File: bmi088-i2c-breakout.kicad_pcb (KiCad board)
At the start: 2 copper layers, 14.2 x 10.5 mm, 9 parts, among them J1 Conn_01x04_Socket, J2 Conn_01x04_Socket, U1 BMI088

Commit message: modified:   bmi088-i2c-breakout.kicad_pcb
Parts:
- moved JP2 2.15 mm to (150.4, 90.9)
- moved U1 0.25 mm to (152.1, 94.5)
- turned JP1 to 180 degrees
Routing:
- net /SCL: track 0.00 -> 15.6 mm, vias 0 -> 2
- net /3V3: track 0.00 -> 15.0 mm, vias 0 -> 2
- net Net-(JP1-B): track 0.00 -> 13.9 mm, vias 0 -> 2
- net /INT1: track 0.00 -> 11.5 mm, vias 0 -> 1
- net /SDA: track 0.00 -> 10.4 mm
- net /GND: track 0.00 -> 9.87 mm, vias 0 -> 2
- net /INT2: track 0.00 -> 9.02 mm, vias 0 -> 1
- net /INT4: track 0.00 -> 8.63 mm, vias 0 -> 1
- net /INT3: track 0.00 -> 8.31 mm, vias 0 -> 1
- net Net-(JP2-B): track 0.00 -> 6.58 mm
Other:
- board size 14.2 x 10.5 mm -> 14.2 x 9.9 mm
- board text added: "J1"
- board text added: "J2"
- board text removed: "SCL"

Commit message: modified:   bmi088-i2c-breakout.kicad_pcb
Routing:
- net /INT3: track 8.31 -> 16.1 mm
- net /SDA: track 10.4 -> 3.51 mm
- net /INT4: track 8.63 -> 9.68 mm
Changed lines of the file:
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@@
 	)
 	(setup
+		(stackup
+			(layer "F.SilkS"
+				(type "Top Silk Screen")
+			)
+			(layer "F.Paste"
+				(type "Top Solder Paste")
+			)
+			(layer "F.Mask"
+				(type "Top Solder Mask")
+				(thickness 0.01)
+			)
+			(layer "F.Cu"
+				(type "copper")
+				(thickness 0.035)
+			)
+			(layer "dielectric 1"
+				(type "core")
+				(thickness 1.51)
+				(material "FR4")
+				(epsilon_r 4.5)
+				(loss_tangent 0.02)
+			)
+			(layer "B.Cu"
+				(type "copper")
+				(thickness 0.035)
+			)
+			(layer "B.Mask"
+				(type "Bottom Solder Mask")
+				(thickness 0.01)
+			)
+			(layer "B.Paste"
+				(type "Bottom Solder Paste")
+			)
+			(layer "B.SilkS"
+				(type "Bottom Silk Screen")
+			)
+			(copper_finish "None")
+			(dielectric_constraints no)
+		)
 		(pad_to_mask_clearance 0)
 		(allow_soldermask_bridges_in_footprints no)
@@
 		(capping no)
 		(filling no)
+		(zone_defaults)
 		(pcbplotparams
 			(layerselection 0x00000000_00000000_55555555_5755f5ff)
@@
 	)
 	(segment
-		(start 153.625 97.6)
-		(end 153.625 95.725)
-		(width 0.2)
-		(layer "F.Cu")
-		(net "/SDA")
-	)
-	(segment
 		(start 148.625 97.725)
 		(end 148.625 97.924999)
@@
 	)
 	(segment
-		(start 153.5 97.725)
-		(end 153.625 97.6)
-		(width 0.2)
-		(layer "F.Cu")
-		(net "/SDA")
-	)
-	(segment
 		(start 148.625 97.924999)
 		(end 148.304999 98.245)
-		(width 0.2)
-		(layer "F.Cu")
-		(net "/SDA")
-	)
-	(segment
-		(start 148.625 97.725)
-		(end 153.5 97.725)
 		(width 0.2)
 		(layer "F.Cu")
@@
 	)
 	(segment
+		(start 156.98 97.725)
+		(end 159 95.705)
+		(width 0.2)
+		(layer "F.Cu")
+		(net "/INT3")
+	)
+	(segment
+		(start 152.675 97.725)
+		(end 156.98 97.725)
+		(width 0.2)
+		(layer "F.Cu")
+		(net "/INT3")
+	)
+	(segment
 		(start 152.125 95.725)
 		(end 152.125 96.55)
@@
 	)
 	(segment
+		(start 152.7 97.7)
+		(end 152.675 97.725)
+		(width 0.2)
+		(layer "F.Cu")
+		(net "/INT3")
+	)
+	(segment
+		(start 152.7 97.125)
+		(end 152.7 97.7)
+		(width 0.2)
+		(layer "F.Cu")
+		(net "/INT3")
+	)
+	(segment
 		(start 152.125 96.55)
 		(end 152.7 97.125)
@@
 	)
 	(via
-		(at 152.675 97.15)
+		(at 152.675 97.725)
 		(size 0.6)
 		(drill 0.3)
@@
 	(segment
 		(start 151.625 95.725)
-		(end 151.625 97.1)
+		(end 151.625 97.7)
 		(width 0.2)
 		(layer "F.Cu")
 		(net "/INT4")
 	)
+	(segment
+		(start 151.625 97.7)
+		(end 151.6 97.725)
+		(width 0.2)
+		(layer "F.Cu")
+		(net "/INT4")
+	)
+	(segment
+		(start 158.94 98.305)
+		(end 159 98.245)
+		(width 0.2)
+		(layer "F.Cu")
+		(net "/INT4")
+	)
+	(segment
+		(start 152.18 98.305)
+		(end 158.94 98.305)
+		(width 0.2)
+		(layer "F.Cu")
+		(net "/INT4")
+	)
+	(segment
+		(start 151.6 97.725)
+		(end 152.18 98.305)
+		(width 0.2)
+		(layer "F.Cu")
+		(net "/INT4")
+	)
 	(via
-		(at 151.6 97.15)
+		(at 151.6 97.725)
 		(size 0.6)
 		(drill 0.3)
@@
 		(net "/INT4")
 	)
-	(segment
-		(start 152.695 98.245)
-		(end 158.4 98.245)
-		(width 0.2)
-		(layer "B.Cu")
-		(net "/INT4")
-	)
-	(segment
-		(start 151.6 97.15)
-		(end 152.695 98.245)
-		(width 0.2)
-		(layer "B.Cu")
-		(net "/INT4")
-	)

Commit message: modified:   bmi088-i2c-breakout.kicad_pcb
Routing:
- net /SDA: track 3.51 -> 12.8 mm, vias 0 -> 2
- net /INT3: track 16.1 -> 11.0 mm, vias 1 -> 0
- net /INT4: track 9.68 -> 9.65 mm, vias 1 -> 0
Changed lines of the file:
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@@
+	)
+	(segment
+		(start 154.875 96.975)
+		(end 154.875 97.225)
+		(width 0.2)
+		(layer "F.Cu")
+		(net "/SDA")
+	)
+	(segment
+		(start 149.55 98.775)
+		(end 148.699999 97.924999)
+		(width 0.2)
+		(layer "F.Cu")
+		(net "/SDA")
+	)
+	(segment
+		(start 148.699999 97.924999)
+		(end 148.625 97.924999)
+		(width 0.2)
+		(layer "F.Cu")
+		(net "/SDA")
 	)
 	(segment
@@
 	)
 	(segment
+		(start 153.625 95.725)
+		(end 154.875 96.975)
+		(width 0.2)
+		(layer "F.Cu")
+		(net "/SDA")
+	)
+	(via
+		(at 149.55 98.775)
+		(size 0.6)
+		(drill 0.3)
+		(layers "F.Cu" "B.Cu")
+		(net "/SDA")
+	)
+	(via
+		(at 154.875 97.225)
+		(size 0.6)
+		(drill 0.3)
+		(layers "F.Cu" "B.Cu")
+		(net "/SDA")
+	)
+	(segment
+		(start 154.875 97.225)
+		(end 153.325 98.775)
+		(width 0.2)
+		(layer "B.Cu")
+		(net "/SDA")
+	)
+	(segment
+		(start 153.325 98.775)
+		(end 149.55 98.775)
+		(width 0.2)
+		(layer "B.Cu")
+		(net "/SDA")
+	)
+	(segment
 		(start 147.11 96.85)
 		(end 147.985 97.725)
@@
 	)
 	(segment
-		(start 156.98 97.725)
-		(end 159 95.705)
-		(width 0.2)
-		(layer "F.Cu")
-		(net "/INT3")
-	)
-	(segment
-		(start 152.675 97.725)
-		(end 156.98 97.725)
+		(start 153.5 97.925)
+		(end 156.78 97.925)
+		(width 0.2)
+		(layer "F.Cu")
+		(net "/INT3")
+	)
+	(segment
+		(start 152.125 96.55)
+		(end 153.5 97.925)
 		(width 0.2)
 		(layer "F.Cu")
@@
 	)
 	(segment
-		(start 152.7 97.7)
-		(end 152.675 97.725)
-		(width 0.2)
-		(layer "F.Cu")
-		(net "/INT3")
-	)
-	(segment
-		(start 152.7 97.125)
-		(end 152.7 97.7)
-		(width 0.2)
-		(layer "F.Cu")
-		(net "/INT3")
-	)
-	(segment
-		(start 152.125 96.55)
-		(end 152.7 97.125)
-		(width 0.2)
-		(layer "F.Cu")
-		(net "/INT3")
-	)
-	(via
-		(at 152.675 97.725)
-		(size 0.6)
-		(drill 0.3)
-		(layers "F.Cu" "B.Cu")
-		(net "/INT3")
-	)
-	(segment
-		(start 152.675 97.15)
-		(end 157.555 97.15)
-		(width 0.2)
-		(layer "B.Cu")
+		(start 156.78 97.925)
+		(end 159 95.705)
+		(width 0.2)
+		(layer "F.Cu")
 		(net "/INT3")
 	)
@@
 	)
 	(segment
+		(start 152.18 98.305)
+		(end 158.94 98.305)
+		(width 0.2)
+		(layer "F.Cu")
+		(net "/INT4")
+	)
+	(segment
 		(start 151.625 95.725)
-		(end 151.625 97.7)
-		(width 0.2)
-		(layer "F.Cu")
-		(net "/INT4")
-	)
-	(segment
-		(start 151.625 97.7)
-		(end 151.6 97.725)
+		(end 151.625 97.75)
+		(width 0.2)
+		(layer "F.Cu")
+		(net "/INT4")
+	)
+	(segment
+		(start 151.625 97.75)
+		(end 152.18 98.305)
 		(width 0.2)
 		(layer "F.Cu")
@@
 		(net "/INT4")
 	)
-	(segment
-		(start 152.18 98.305)
-		(end 158.94 98.305)
-		(width 0.2)
-		(layer "F.Cu")
-		(net "/INT4")
-	)
-	(segment
-		(start 151.6 97.725)
-		(end 152.18 98.305)
-		(width 0.2)
-		(layer "F.Cu")
-		(net "/INT4")
-	)
-	(via
-		(at 151.6 97.725)
-		(size 0.6)
-		(drill 0.3)
-		(layers "F.Cu" "B.Cu")
-		(net "/INT4")
-	)

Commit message: modified:   bmi088-i2c-breakout.kicad_pcb
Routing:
- net /3V3: track 15.0 -> 25.9 mm
- added copper zone on F.Cu, net /GND
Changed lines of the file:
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@@
 	)
 	(segment
-		(start 153.625 92.4)
+		(start 152.67 89.595)
+		(end 153.6 90.525)
+		(width 0.2)
+		(layer "F.Cu")
+		(net "/3V3")
+	)
+	(segment
+		(start 145.855 89.595)
+		(end 152.67 89.595)
+		(width 0.2)
+		(layer "F.Cu")
+		(net "/3V3")
+	)
+	(segment
+		(start 153.625 91.83)
 		(end 153.625 93.2)
+		(width 0.2)
+		(layer "F.Cu")
+		(net "/3V3")
+	)
+	(segment
+		(start 153.6 91.805)
+		(end 153.625 91.83)
+		(width 0.2)
+		(layer "F.Cu")
+		(net "/3V3")
+	)
+	(segment
+		(start 153.6 90.525)
+		(end 153.6 91.805)
 		(width 0.2)
 		(layer "F.Cu")
@@
 	)
 	(segment
-		(start 153.625 91.83)
-		(end 153.625 92.4)
-		(width 0.2)
-		(layer "F.Cu")
-		(net "/3V3")
-	)
-	(segment
 		(start 146.96 91.84)
 		(end 147.035 91.915)
@@
 	)
 	(segment
+		(start 144.825 90.625)
+		(end 145.855 89.595)
+		(width 0.2)
+		(layer "F.Cu")
+		(net "/3V3")
+	)
+	(segment
 		(start 147.035 92.715)
 		(end 147.025 92.725)
@@
 		(net "/INT1")
 	)
+	(zone
+		(net "/GND")
+		(layer "F.Cu")
+		(hatch edge 0.5)
+		(connect_pads
+			(clearance 0.5)
+		)
+		(min_thickness 0.25)
+		(fill yes
+			(thermal_gap 0.5)
+			(thermal_bridge_width 0.5)
+			(island_removal_mode 0)
+		)
+		(polygon
+			(pts
+				(xy 144.9 89.45) (xy 159.05 89.475) (xy 159 99.325) (xy 144.875 99.35) (xy 144.875 89.475)
+			)
+		)
+	)
 	(embedded_fonts no)

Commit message: modified:   bmi088-i2c-breakout.kicad_pcb
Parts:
- added G***: LOGO, LOGO, F.Cu at (155.8, 97.7)
- added G***: LOGO, LOGO, B.Cu at (152.6, 94.4)
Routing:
- net /SDA: track 12.8 -> 12.3 mm
- removed copper zone on F.Cu, net /GND
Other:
- board text added: "3V"
- board text added: "CA"
- board text added: "CL"
- board text added: "GD"
- board text added: "I1"
- board text added: "I2"
- board text added: "I3"
- board text added: "I4"
- board text removed: "3V3"
- board text removed: "GND"
- board text removed: "INT1"
- board text removed: "INT2"
- board text removed: "INT3"
- board text removed: "INT4"
- board text removed: "SDA"

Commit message: modified:   bmi088-i2c-breakout.kicad_pcb
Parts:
- moved G*** 1.17 mm to (151.8, 93.6)
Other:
- board text added: "tindie.com/stores/bobbiebots"

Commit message: modified:   bmi088-i2c-breakout.kicad_pcb
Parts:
- moved R1 8.39 mm to (155.4, 92.0), turned to -90 degrees
- moved JP1 8.18 mm to (154.4, 98.8), turned to 0 degrees
- moved G*** 8.15 mm to (147.9, 95.5)
- moved R2 7.95 mm to (156.2, 98.8)
- moved JP2 4.48 mm to (154.9, 90.7)
- moved C2 3.20 mm to (148.4, 97.8)
- moved C1 3.10 mm to (150.3, 90.5), turned to 180 degrees
- moved G*** 1.03 mm to (152.5, 94.3)
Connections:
- J1 pad 1: /INT1 -> /3V3
- J1 pad 2: /INT2 -> /SCL
- J1 pad 3: /INT3 -> /SDA
- J1 pad 4: /INT4 -> /INT3
- J2 pad 1: /3V3 -> /INT1
- J2 pad 3: /SCL -> /INT2
- J2 pad 4: /SDA -> /INT4
- U1 pad 11: /VDDIO -> /3V3
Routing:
- net /3V3: track 25.9 -> 50.5 mm, vias 2 -> 6
- net /GND: track 9.87 -> 31.0 mm, vias 2 -> 0
- net Net-(JP1-B): track 13.9 -> 1.11 mm, vias 2 -> 0
- net /SCL: track 15.6 -> 8.12 mm, vias 2 -> 0
- net Net-(JP2-B): track 6.58 -> 1.04 mm
- net /SDA: track 12.3 -> 9.56 mm, vias 2 -> 0
- net /INT2: track 9.02 -> 6.84 mm
- net /INT1: track 11.5 -> 9.62 mm, vias 1 -> 2
- net /INT4: track 9.65 -> 8.28 mm, vias 0 -> 1
- net /INT3: track 11.0 -> 10.0 mm, vias 0 -> 1
- added copper zone on F.Cu, net /GND
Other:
- board size 14.2 x 9.9 mm -> 14.2 x 10.1 mm
- board text added: "DA"
- board text removed: "CA"

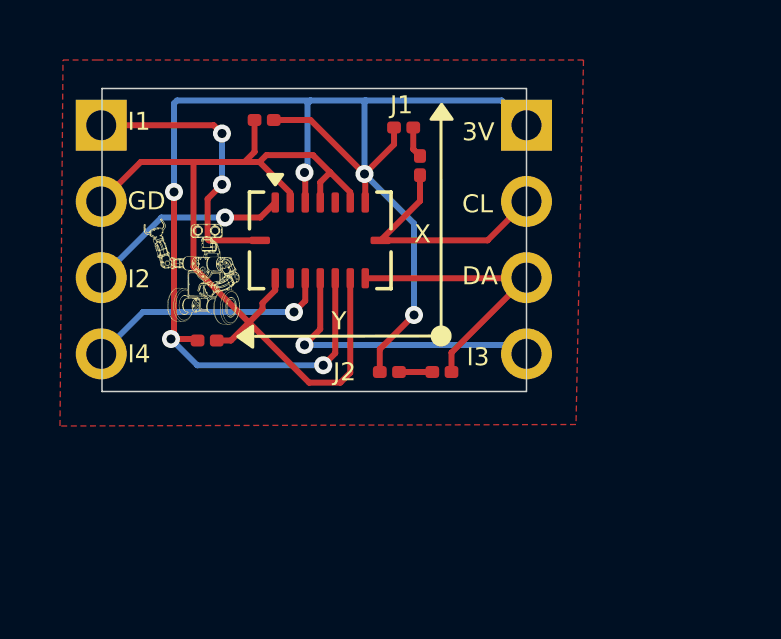
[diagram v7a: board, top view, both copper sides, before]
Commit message: Fixed mis-labeled resistors
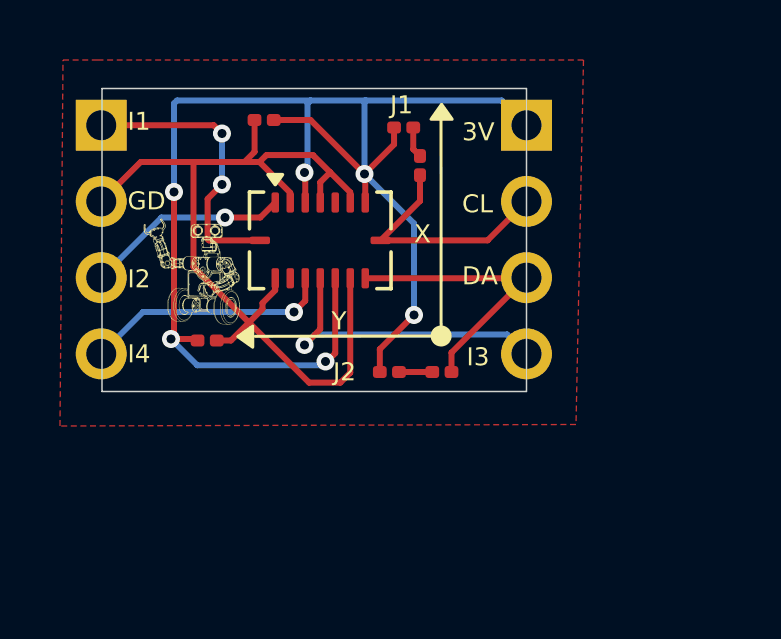
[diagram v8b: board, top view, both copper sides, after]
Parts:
- JP1: renamed from JP2; value Jumper_2_Open -> Jumper_1_Open
- R1, R2: footprint Capacitor_SMD:C_0201_0603Metric -> Resistor_SMD:R_0201_0603Metric
- renumbered JP1 to JP2
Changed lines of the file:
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@@
 		(capping no)
 		(filling no)
+		(zone_defaults)
 		(pcbplotparams
 			(layerselection 0x00000000_00000000_55555555_5755f5ff)
@@
 		(descr "Capacitor SMD 0201 (0603 Metric), square (rectangular) end terminal, IPC-7351 nominal, (Body size source: https://www.vishay.com/docs/20052/crcw0201e3.pdf)")
 		(tags "capacitor")
-		(property "Reference" "JP2"
+		(property "Reference" "JP1"
 			(at 0 -1.05 0)
 			(layer "F.SilkS")
@@
 			)
 		)
-		(property "Value" "Jumper_2_Open"
+		(property "Value" "Jumper_1_Open"
 			(at 0 1.05 0)
 			(layer "F.Fab")
@@
 			)
 		)
-		(attr smd)
+		(attr smd dnp)
 		(duplicate_pad_numbers_are_jumpers no)
 		(fp_rect
@@
 			(layers "F.Cu" "F.Mask")
 			(roundrect_rratio 0.25)
-			(net "Net-(JP2-B)")
+			(net "Net-(JP1-B)")
 			(pinfunction "B_2")
 			(pintype "passive")
@@
 		)
 	)
-	(footprint "Capacitor_SMD:C_0201_0603Metric"
+	(footprint "Resistor_SMD:R_0201_0603Metric"
 		(layer "F.Cu")
 		(at 155.45 91.97 -90)
-		(descr "Capacitor SMD 0201 (0603 Metric), square (rectangular) end terminal, IPC-7351 nominal, (Body size source: https://www.vishay.com/docs/20052/crcw0201e3.pdf)")
-		(tags "capacitor")
+		(descr "Resistor SMD 0201 (0603 Metric), square (rectangular) end terminal, IPC-7351 nominal, (Body size source: https://www.vishay.com/docs/20052/crcw0201e3.pdf)")
+		(tags "resistor")
 		(property "Reference" "R1"
-			(at 0 -1.05 90)
+			(at 0 -1.05 270)
 			(layer "F.SilkS")
 			(hide yes)
@@
 		)
 		(property "Value" "1.5kΩ"
-			(at 0 1.05 90)
+			(at 0 1.05 270)
 			(layer "F.Fab")
 			(hide yes)
@@
 		)
 		(property "Datasheet" ""
-			(at 0 0 90)
+			(at 0 0 270)
 			(layer "F.Fab")
 			(hide yes)
@@
 		)
 		(property "Description" "Resistor"
-			(at 0 0 90)
+			(at 0 0 270)
 			(layer "F.Fab")
 			(hide yes)
@@
 		)
 		(property "KiLib_Generator" "SMD_2terminal_chip_molded"
-			(at 0 0 90)
+			(at 0 0 270)
 			(layer "F.SilkS")
 			(hide yes)
@@
 		)
 		(fp_text user "${REFERENCE}"
-			(at 0 0.6 90)
+			(at 0 -0.68 270)
 			(layer "F.Fab")
 			(effects
@@
 			(layers "F.Cu" "F.Mask")
 			(roundrect_rratio 0.25)
-			(net "Net-(JP2-B)")
+			(net "Net-(JP1-B)")
 			(pintype "passive")
 		)
@@
 		)
 		(embedded_fonts no)
-		(model "${KICAD10_3DMODEL_DIR}/Capacitor_SMD.3dshapes/C_0201_0603Metric.step"
+		(model "${KICAD10_3DMODEL_DIR}/Resistor_SMD.3dshapes/R_0201_0603Metric.step"
 			(offset
 				(xyz 0 0 0)
@@
 		(descr "Capacitor SMD 0201 (0603 Metric), square (rectangular) end terminal, IPC-7351 nominal, (Body size source: https://www.vishay.com/docs/20052/crcw0201e3.pdf)")
 		(tags "capacitor")
-		(property "Reference" "JP1"
+		(property "Reference" "JP2"
 			(at 0 -1.05 0)
 			(layer "F.SilkS")
@@
 			)
 		)
-		(attr smd)
+		(attr smd dnp)
 		(duplicate_pad_numbers_are_jumpers no)
 		(fp_rect
@@
 			(layers "F.Cu" "F.Mask")
 			(roundrect_rratio 0.25)
-			(net "Net-(JP1-B)")
+			(net "Net-(JP2-B)")
 			(pinfunction "B_2")
 			(pintype "passive")
@@
 		)
 	)
-	(footprint "Capacitor_SMD:C_0201_0603Metric"
+	(footprint "Resistor_SMD:R_0201_0603Metric"
 		(layer "F.Cu")
 		(at 156.18 98.85)
-		(descr "Capacitor SMD 0201 (0603 Metric), square (rectangular) end terminal, IPC-7351 nominal, (Body size source: https://www.vishay.com/docs/20052/crcw0201e3.pdf)")
-		(tags "capacitor")
+		(descr "Resistor SMD 0201 (0603 Metric), square (rectangular) end terminal, IPC-7351 nominal, (Body size source: https://www.vishay.com/docs/20052/crcw0201e3.pdf)")
+		(tags "resistor")
 		(property "Reference" "R2"
 			(at 0 -1.05 0)
@@
 			(layers "F.Cu" "F.Mask")
 			(roundrect_rratio 0.25)
-			(net "Net-(JP1-B)")
+			(net "Net-(JP2-B)")
 			(pintype "passive")
 		)
@@
 		)
 		(embedded_fonts no)
-		(model "${KICAD10_3DMODEL_DIR}/Capacitor_SMD.3dshapes/C_0201_0603Metric.step"
+		(model "${KICAD10_3DMODEL_DIR}/Resistor_SMD.3dshapes/R_0201_0603Metric.step"
 			(offset
 				(xyz 0 0 0)
@@
 	)
 	(segment
-		(start 152.225 98.625)
-		(end 152.15 98.7)
-		(width 0.2)
-		(layer "F.Cu")
-		(net "/3V3")
-	)
-	(segment
 		(start 147.25 97.65)
 		(end 147.15 97.75)
@@
 	)
 	(via
-		(at 152.225 98.625)
+		(at 152.3 98.5)
 		(size 0.6)
 		(drill 0.3)
@@
 	)
 	(segment
-		(start 155.225 90.7)
-		(end 155.225 91.425)
-		(width 0.2)
-		(layer "F.Cu")
-		(net "Net-(JP2-B)")
-	)
-	(segment
-		(start 155.225 91.425)
-		(end 155.45 91.65)
+		(start 154.75 98.85)
+		(end 155.86 98.85)
 		(width 0.2)
 		(layer "F.Cu")
@@
 	)
 	(segment
-		(start 154.75 98.85)
-		(end 155.86 98.85)
+		(start 155.225 90.7)
+		(end 155.225 91.425)
+		(width 0.2)
+		(layer "F.Cu")
+		(net "Net-(JP1-B)")
+	)
+	(segment
+		(start 155.225 91.425)
+		(end 155.45 91.65)
 		(width 0.2)
 		(layer "F.Cu")
@@
 	(segment
 		(start 151.6 97.95)
-		(end 158.705 97.95)
+		(end 151.95 97.6)
+		(width 0.2)
+		(layer "B.Cu")
+		(net "/INT3")
+	)
+	(segment
+		(start 151.95 97.6)
+		(end 158.355 97.6)
 		(width 0.2)
 		(layer "B.Cu")
@@
 	)
 	(segment
-		(start 158.705 97.95)
+		(start 158.355 97.6)
 		(end 159 98.245)
 		(width 0.2)
